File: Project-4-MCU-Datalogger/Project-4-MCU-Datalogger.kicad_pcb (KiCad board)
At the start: 2 copper layers, 51.9 x 33.4 mm, 30 parts, among them J1 Conn_01x04_Pin, J2 Conn_01x04_Pin, J3 Conn_01x09_Pin, J4 Conn_02x03_Odd_Even, U1 24LC1025, U2 24LC1025, U3 DS1337S_, U4 ATMEGA328P-AU, Y1 16 MHz, Y2 32.768 KHz

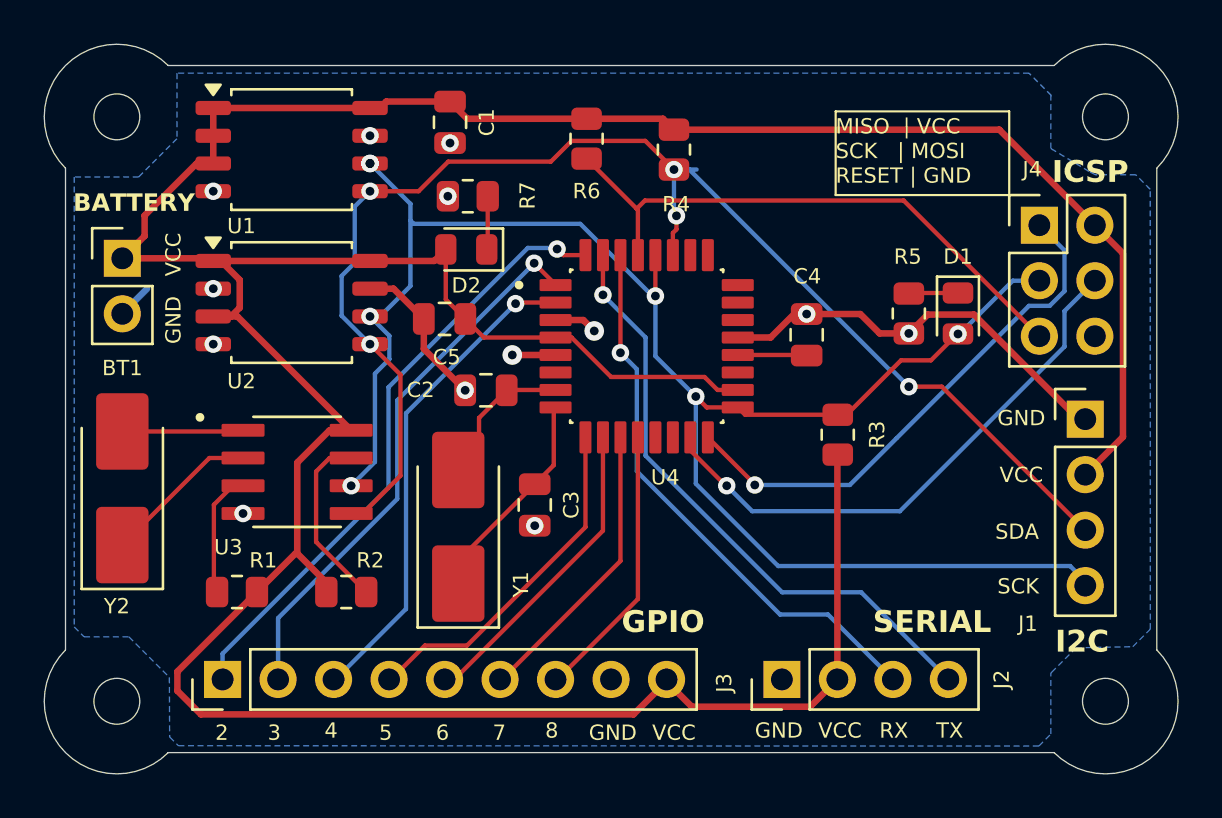
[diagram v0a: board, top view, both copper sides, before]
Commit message: remove all zones, tracks and vias and change PCB to 4 layers
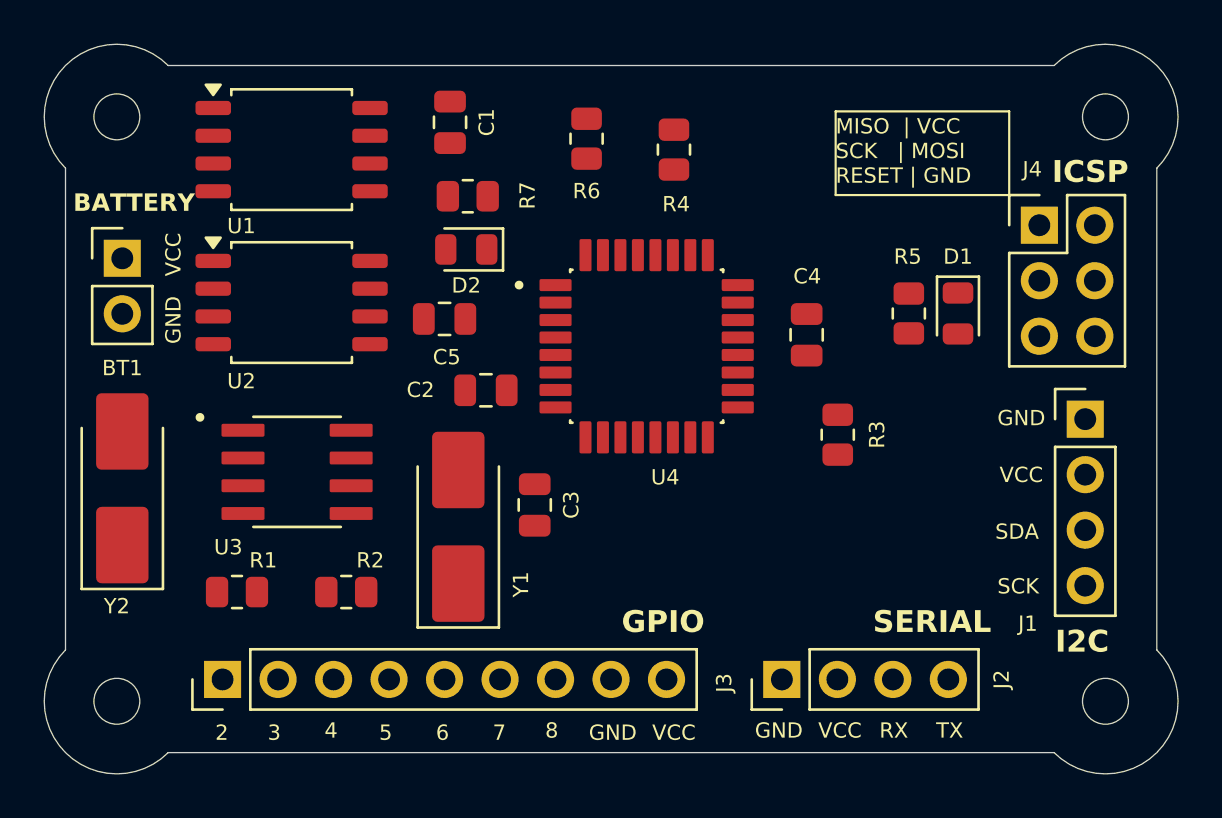
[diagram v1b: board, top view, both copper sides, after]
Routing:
- net /Vcc: track 171.1 -> 0.00 mm
- net /SCK: track 80.0 -> 0.00 mm, vias 9 -> 0
- net /SDA: track 64.0 -> 0.00 mm, vias 5 -> 0
- net GND: track 31.8 -> 0.00 mm, vias 18 -> 0
- net /D2: track 28.4 -> 0.00 mm, vias 2 -> 0
- net /TX: track 28.1 -> 0.00 mm, vias 2 -> 0
- net /RESET: track 26.6 -> 0.00 mm
- net /RX: track 25.9 -> 0.00 mm, vias 2 -> 0
- net /MOSI: track 25.6 -> 0.00 mm, vias 3 -> 0
- net /D3: track 25.4 -> 0.00 mm, vias 2 -> 0
- net /MISO: track 24.4 -> 0.00 mm, vias 2 -> 0
- net /D4: track 22.6 -> 0.00 mm, vias 2 -> 0
- net /D5: track 16.0 -> 0.00 mm
- net /D6: track 14.4 -> 0.00 mm
- net /D7: track 13.5 -> 0.00 mm
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- removed copper zone on B.Cu, net GND
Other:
- copper layers 2 -> 4

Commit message: route on all 4 layers, run and clear DRC
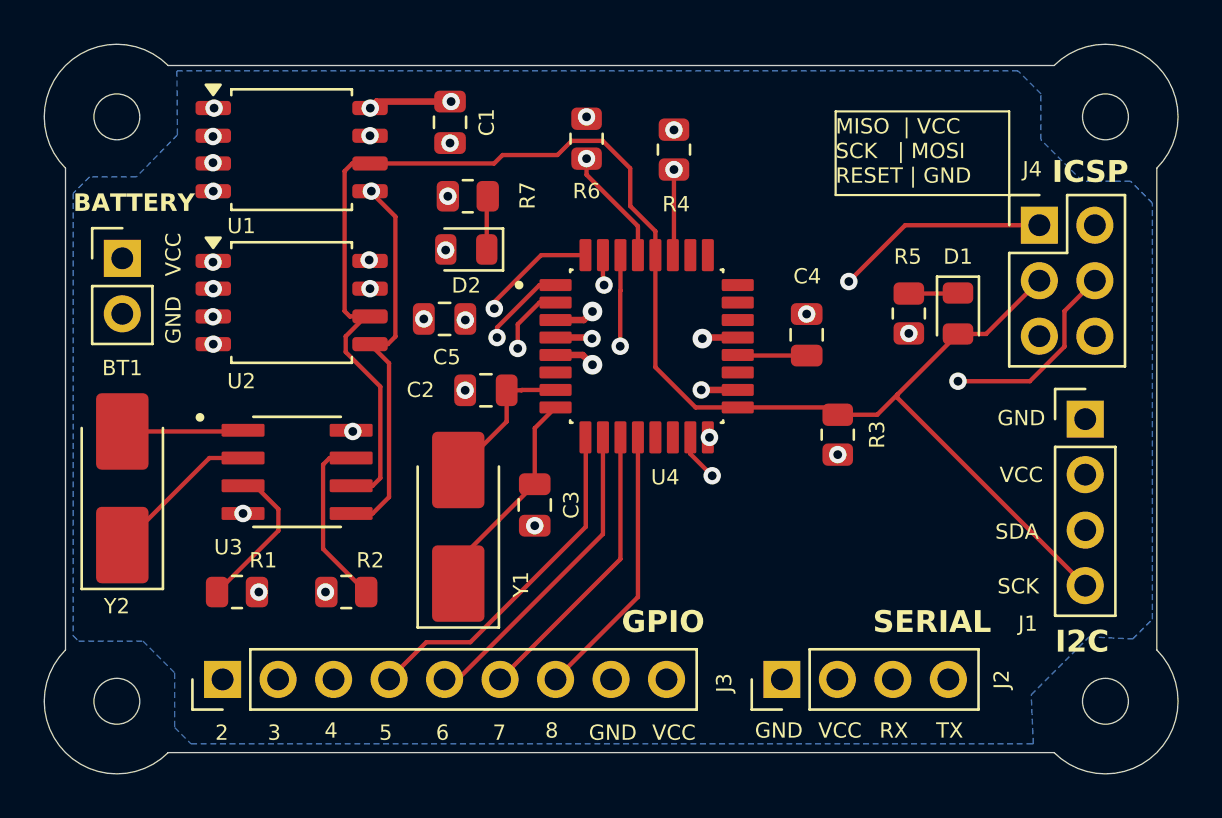
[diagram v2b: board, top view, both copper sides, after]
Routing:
- net /SCK: track 0.00 -> 74.9 mm
- net /SDA: track 0.00 -> 63.1 mm, vias 0 -> 3
- net /RESET: track 0.00 -> 29.6 mm, vias 0 -> 2
- net /TX: track 0.00 -> 27.5 mm, vias 0 -> 2
- net /D2: track 0.00 -> 27.5 mm, vias 0 -> 2
- net /RX: track 0.00 -> 25.1 mm, vias 0 -> 2
- net /MOSI: track 0.00 -> 24.3 mm, vias 0 -> 2
- net /D3: track 0.00 -> 23.7 mm, vias 0 -> 2
- net /D4: track 0.00 -> 21.9 mm, vias 0 -> 2
- net /MISO: track 0.00 -> 20.8 mm, vias 0 -> 2
- net /D5: track 0.00 -> 16.0 mm
- net /D6: track 0.00 -> 14.4 mm
- net /D7: track 0.00 -> 13.4 mm
- net /D8: track 0.00 -> 12.6 mm
- net /Vcc: track 0.00 -> 10.1 mm, vias 0 -> 23
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- added copper zone on In2.Cu, net /Vcc
- added copper zone on B.Cu, net GND

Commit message: bugfix SCL vs SCK misnomer
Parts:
- removed REF**: KiCad-Logo2_5mm_SilkScreen, Symbol:KiCad-Logo2_5mm_SilkScreen
- moved R3 12.5 mm to (81.5, 54.8)
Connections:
- J1 pad 4: /SCK -> /SCL
- R3 pad 2: /SCK -> /SCL
- U1 pad 6: /SCK -> /SCL
- U2 pad 6: /SCK -> /SCL
- U3 pad 6: /SCK -> /SCL
- U4 pad 28: /SCK -> /SCL
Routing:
- net /SCL: track 0.00 -> 83.3 mm
- net /SCK: track 74.9 -> 16.2 mm
- net /MISO: track 20.8 -> 22.6 mm, vias 2 -> 0
- net /TX: track 27.5 -> 26.0 mm, vias 2 -> 1
- net Net-(U3-~{INTA}): track 7.02 -> 6.04 mm
- net /RX: track 25.1 -> 24.6 mm, vias 2 -> 1
- net /MOSI: vias 2 -> 0
- net GND: vias 21 -> 16
- net /Vcc: vias 23 -> 18
- net /SDA: vias 3 -> 2
- net /RESET: vias 2 -> 1
- net /D4: vias 2 -> 1
- net /D3: vias 2 -> 1
- net /D2: vias 2 -> 1

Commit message: add jquk logo to front and back silkscreens
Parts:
- added G***: LOGO, logos:jquk_logo_10mm_bw, F.Cu at (87.2, 68.0)
- added G***: LOGO, logos:jquk_logo_10mm_bw, B.Cu at (61.2, 65.0)

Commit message: minor change on jquk-logo
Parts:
- renumbered G*** to jquk-logo
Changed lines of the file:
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@@
 		(layer "F.Cu")
 		(at 87.25 68)
-		(property "Reference" "G***"
+		(property "Reference" "jquk-logo"
 			(at 0 0 0)
 			(layer "F.SilkS")

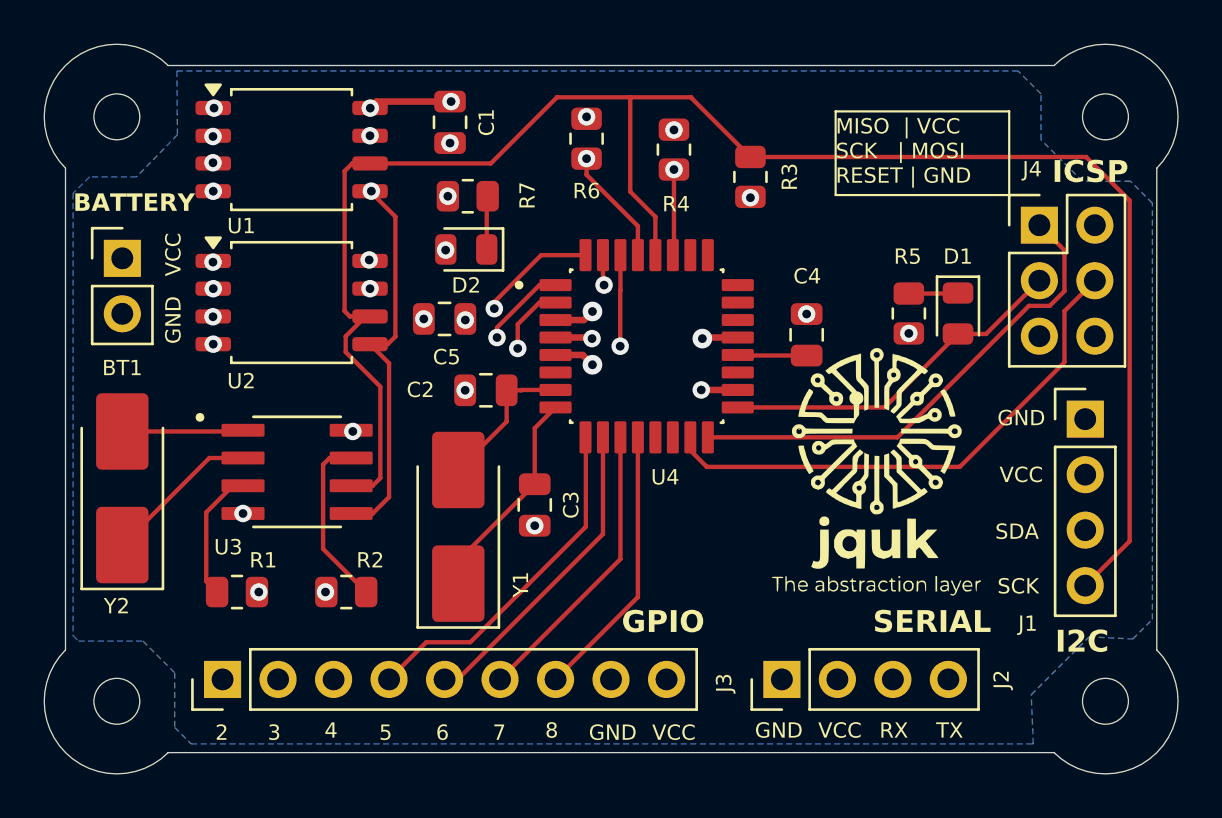
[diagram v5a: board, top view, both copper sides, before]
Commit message: delete all zones, tracks, vias before autorouting
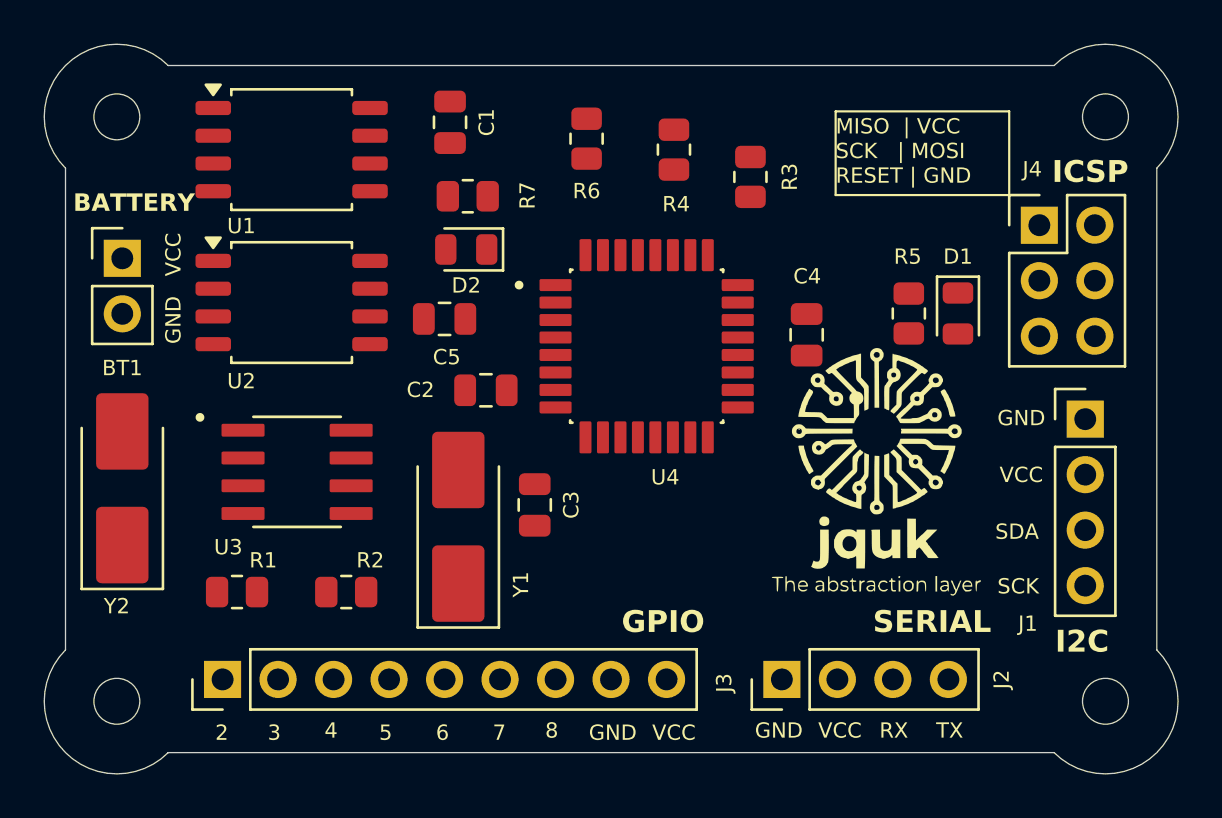
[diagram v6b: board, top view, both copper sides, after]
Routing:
- net /SCL: track 83.3 -> 0.00 mm
- net /SDA: track 63.1 -> 0.00 mm, vias 2 -> 0
- net /RESET: track 29.6 -> 0.00 mm, vias 1 -> 0
- net /D2: track 27.5 -> 0.00 mm, vias 1 -> 0
- net /TX: track 26.0 -> 0.00 mm, vias 1 -> 0
- net /RX: track 24.6 -> 0.00 mm, vias 1 -> 0
- net /MOSI: track 24.3 -> 0.00 mm
- net /D3: track 23.7 -> 0.00 mm, vias 1 -> 0
- net /MISO: track 22.6 -> 0.00 mm
- net /D4: track 21.9 -> 0.00 mm, vias 1 -> 0
- net /SCK: track 16.2 -> 0.00 mm
- net /D5: track 16.0 -> 0.00 mm
- net /D6: track 14.4 -> 0.00 mm
- net /D7: track 13.4 -> 0.00 mm
- net /D8: track 12.6 -> 0.00 mm
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- removed copper zone on In2.Cu, net /Vcc
- removed copper zone on B.Cu, net GND

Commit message: autorouted with 'Freerouting' plugin (contains DRC errors)
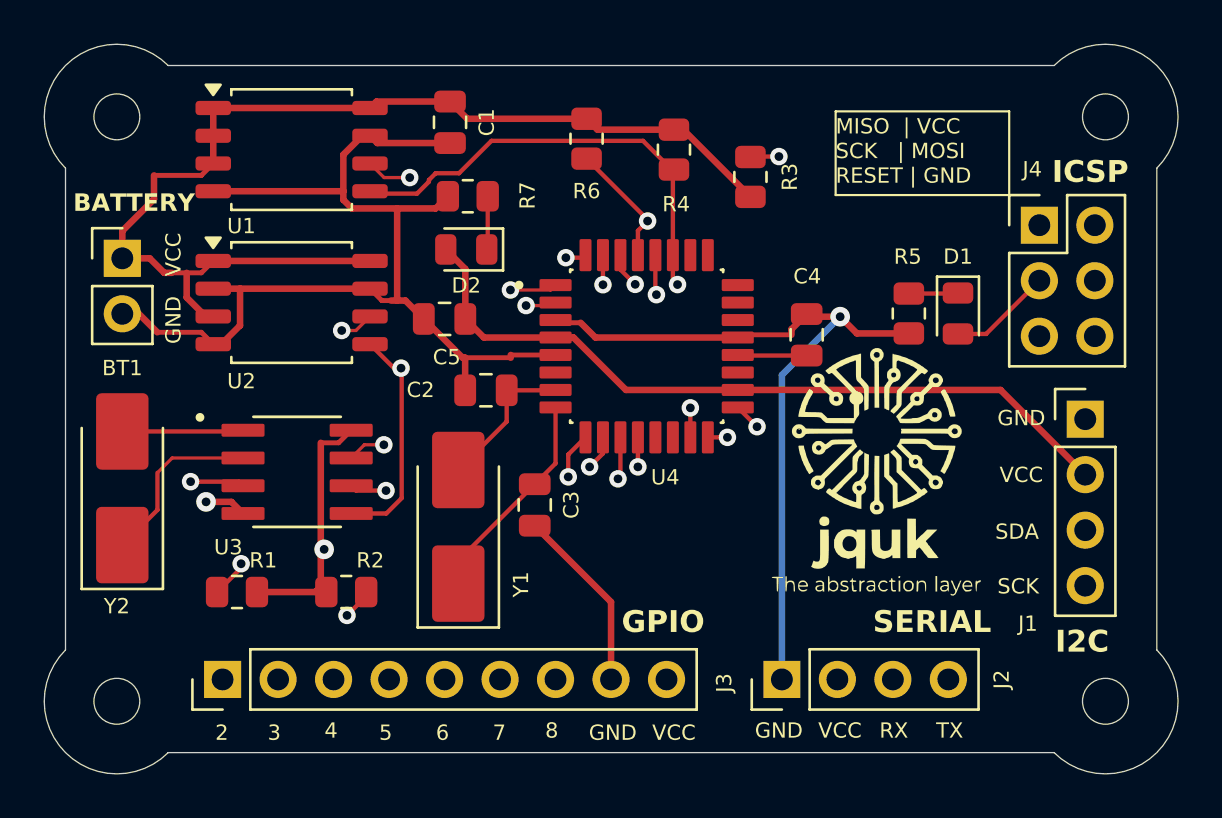
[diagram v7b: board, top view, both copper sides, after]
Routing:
- net /Vcc: track 0.00 -> 173.5 mm, vias 0 -> 1
- net GND: track 0.00 -> 152.6 mm, vias 0 -> 2
- net /SCL: track 0.00 -> 85.2 mm, vias 0 -> 5
- net /SDA: track 0.00 -> 72.6 mm, vias 0 -> 2
- net /TX: track 0.00 -> 33.1 mm, vias 0 -> 1
- net /D2: track 0.00 -> 31.9 mm, vias 0 -> 1
- net /RX: track 0.00 -> 28.1 mm, vias 0 -> 1
- net /RESET: track 0.00 -> 25.9 mm, vias 0 -> 1
- net /MOSI: track 0.00 -> 25.8 mm, vias 0 -> 1
- net /D3: track 0.00 -> 25.1 mm, vias 0 -> 1
- net /D4: track 0.00 -> 22.2 mm, vias 0 -> 1
- net /SCK: track 0.00 -> 21.7 mm, vias 0 -> 1
- net /MISO: track 0.00 -> 19.3 mm, vias 0 -> 1
- net /D8: track 0.00 -> 16.2 mm, vias 0 -> 1
- net /D5: track 0.00 -> 14.8 mm, vias 0 -> 1
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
